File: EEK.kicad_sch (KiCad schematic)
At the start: 40 parts, among them J1 Screw_Terminal_01x02

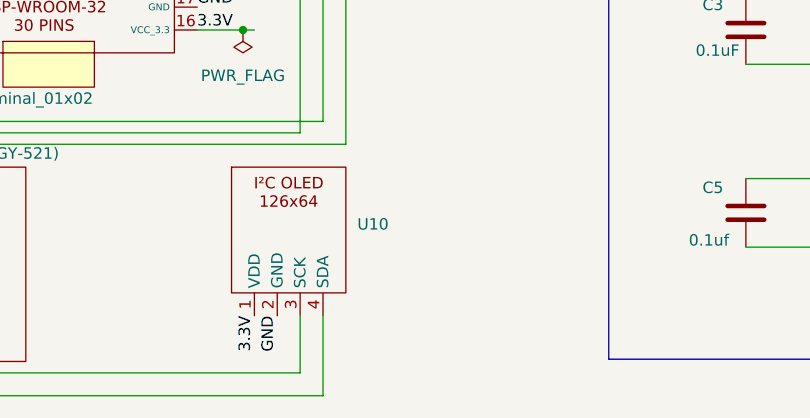
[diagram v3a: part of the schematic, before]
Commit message: add footprint for oled with gnd on pin 1, improve the copper field
Add a second footprint for oled with the gnd on pin 1 instead pin 2. Improve the copper filed
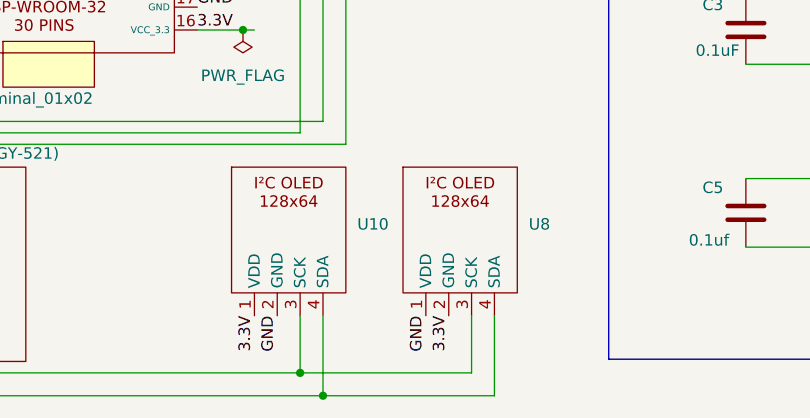
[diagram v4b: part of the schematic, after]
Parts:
- added U8: ~, Connector_PinHeader_2.54mm:PinHeader_1x04_P2.54mm_Vertical, symbol PH_LIB_sym:126x64_I²C_OLED
- U10: footprint TerminalBlock_Phoenix:TerminalBlock_Phoenix_MKDS-1,5-4_1x04_P5.00mm_Horizontal -> Connector_PinHeader_2.54mm:PinHeader_1x04_P2.54mm_Vertical
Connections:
- net 3.3V: now also U8.2 (GND)
- net GND: now also U8.1 (VDD)
- net SCL: now also U8.3 (SCK)
- net SDA: now also U8.4 (SDA)
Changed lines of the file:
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@@
 	)
 	(junction
+		(at 127 124.46)
+		(diameter 0)
+		(color 0 0 0 0)
+	)
+	(junction
+		(at 124.46 121.92)
+		(diameter 0)
+		(color 0 0 0 0)
+	)
+	(junction
 		(at 41.91 64.77)
 		(diameter 0)
@@
 	(wire
 		(pts
+			(xy 127 124.46) (xy 146.05 124.46)
+		)
+		(stroke
+			(width 0)
+			(type default)
+		)
+	)
+	(wire
+		(pts
 			(xy 213.36 80.01) (xy 222.25 80.01)
 		)
@@
 	(wire
 		(pts
+			(xy 143.51 121.92) (xy 143.51 115.57)
+		)
+		(stroke
+			(width 0)
+			(type default)
+		)
+	)
+	(wire
+		(pts
+			(xy 146.05 124.46) (xy 146.05 115.57)
+		)
+		(stroke
+			(width 0)
+			(type default)
+		)
+	)
+	(wire
+		(pts
 			(xy 60.96 72.39) (xy 60.96 68.58)
 		)
@@
 	(wire
 		(pts
+			(xy 124.46 121.92) (xy 143.51 121.92)
+		)
+		(stroke
+			(width 0)
+			(type default)
+		)
+	)
+	(wire
+		(pts
 			(xy 43.18 105.41) (xy 50.8 105.41)
 		)
@@
 	)
 	(label "GND"
+		(at 138.43 115.57 270)
+		(fields_autoplaced yes)
+		(effects
+			(font
+				(size 1.27 1.27)
+			)
+			(justify right bottom)
+		)
+	)
+	(label "GND"
 		(at 222.25 81.28 180)
 		(fields_autoplaced yes)
@@
 		)
 	)
+	(label "3.3V"
+		(at 140.97 115.57 270)
+		(fields_autoplaced yes)
+		(effects
+			(font
+				(size 1.27 1.27)
+			)
+			(justify right bottom)
+		)
+	)
 	(label "GND"
 		(at 49.53 105.41 180)
@@
 			)
 		)
-		(property "Footprint" "TerminalBlock_Phoenix:TerminalBlock_Phoenix_MKDS-1,5-4_1x04_P5.00mm_Horizontal"
+		(property "Footprint" "Connector_PinHeader_2.54mm:PinHeader_1x04_P2.54mm_Vertical"
 			(at 118.11 101.6 0)
 			(effects
@@
 					(unit 1)
 				)
+			)
+		)
+	)
+	(symbol
+		(lib_name "126x64_I²C_OLED_1")
+		(lib_id "PH_LIB_sym:126x64_I²C_OLED")
+		(at 137.16 101.6 0)
+		(unit 1)
+		(exclude_from_sim no)
+		(in_bom yes)
+		(on_board yes)
+		(dnp no)
+		(fields_autoplaced yes)
+		(property "Reference" "U8"
+			(at 149.86 105.4099 0)
+			(effects
+				(font
+					(size 1.27 1.27)
+				)
+				(justify left)
+			)
+		)
+		(property "Value" "~"
+			(at 149.86 107.315 0)
+			(effects
+				(font
+					(size 1.27 1.27)
+				)
+				(justify left)
+			)
+		)
+		(property "Footprint" "Connector_PinHeader_2.54mm:PinHeader_1x04_P2.54mm_Vertical"
+			(at 137.16 101.6 0)
+			(effects
+				(font
+					(size 1.27 1.27)
+				)
+				(hide yes)
+			)
+		)
+		(property "Datasheet" ""
+			(at 137.16 101.6 0)
+			(effects
+				(font
+					(size 1.27 1.27)
+				)
+				(hide yes)
+			)
+		)
+		(property "Description" ""
+			(at 137.16 101.6 0)
+			(effects
+				(font
+					(size 1.27 1.27)
+				)
+				(hide yes)
+			)
+		)
+		(pin "3"
+		)
+		(pin "2"
+		)
+		(pin "4"
+		)
+		(pin "1"
+		)
+		(instances
+			(project "EEK"
+				(path "/0a4f8f30-fcea-49ae-bc76-20e4ae5d80ad"
+					(reference "U8")
+					(unit 1)
+				)

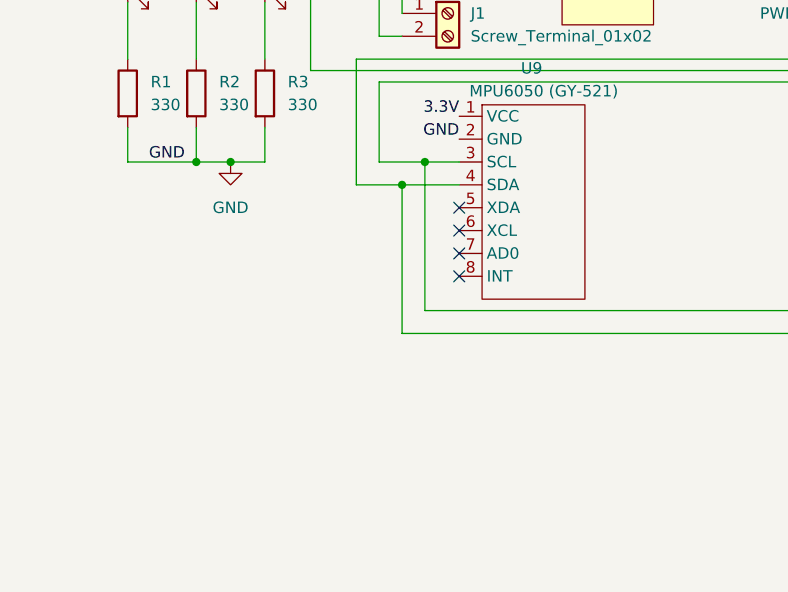
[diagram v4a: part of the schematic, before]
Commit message: improve silkscreen, add capacitors on 3.3V, improve copper filed
improve silkscreen, add capacitors on 3.3V, improve copper filed
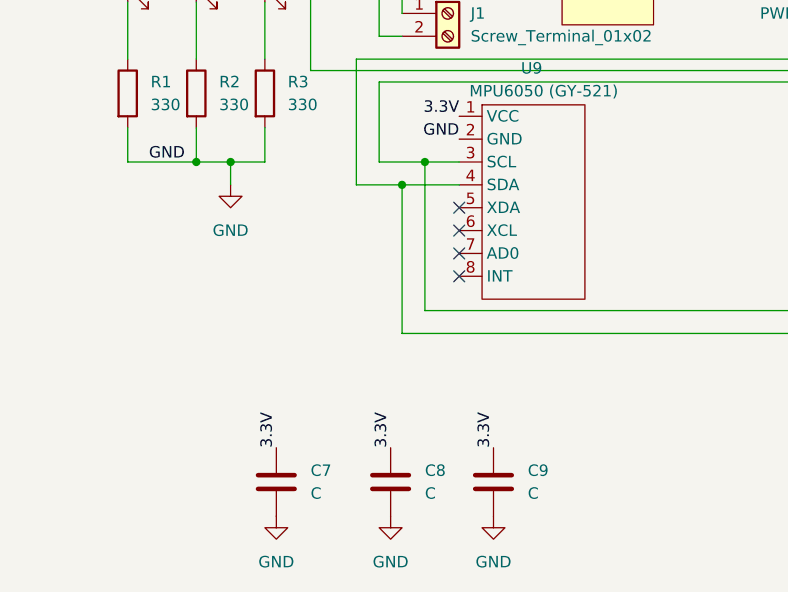
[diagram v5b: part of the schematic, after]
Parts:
- added C7, C8, C9: C, Capacitor_THT:C_Radial_D10.0mm_H12.5mm_P5.00mm, symbol Device:C
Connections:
- net 3.3V: now also C7.1, C8.1, C9.1
- net GND: now also C7.2, C8.2, C9.2

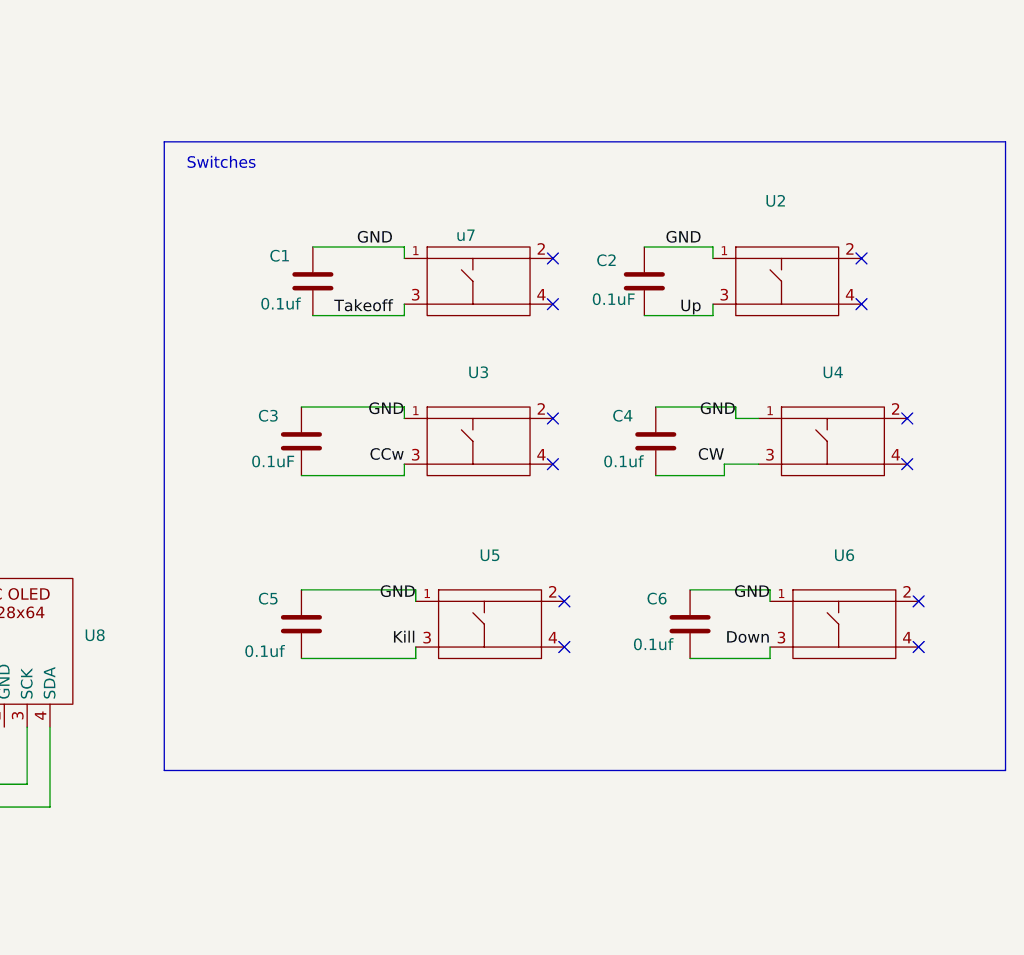
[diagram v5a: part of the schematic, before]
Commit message: add pull down 10K resistors on the switche
add pull down 10K resistors on the switche
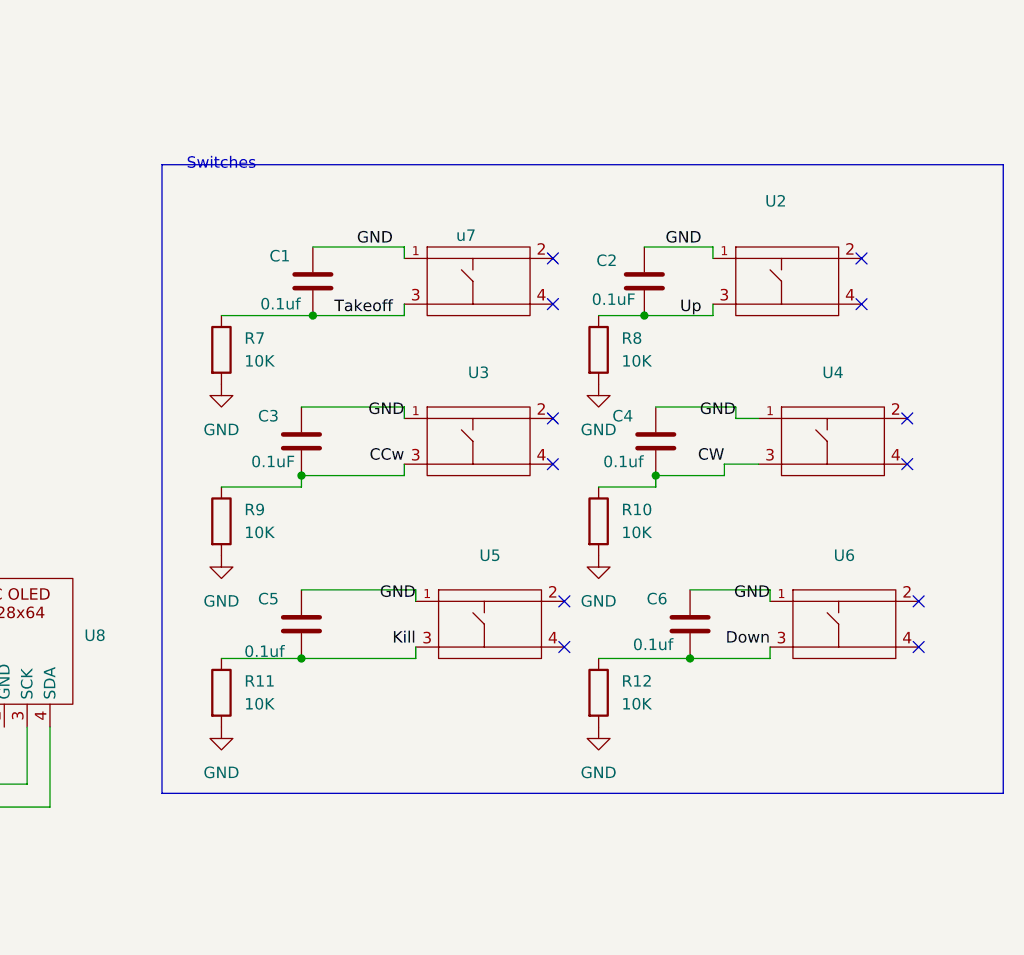
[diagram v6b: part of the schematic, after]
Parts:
- added R10, R11, R12, R7, R8, R9: 10K, Resistor_THT:R_Axial_DIN0207_L6.3mm_D2.5mm_P10.16mm_Horizontal, symbol Device:R
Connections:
- net CCw: now also R9.1
- net CW: now also R10.1
- net Down: now also R12.1
- net GND: now also R10.2, R11.2, R12.2, R7.2, R8.2, R9.2
- net Kill: now also R11.1
- net Takeoff: now also R7.1
- net Up: now also R8.1

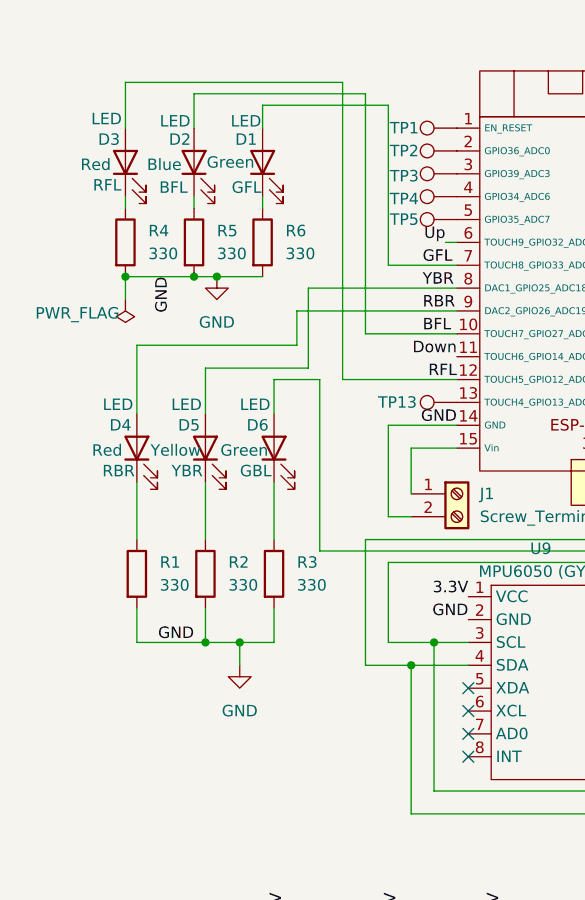
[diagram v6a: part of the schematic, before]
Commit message: Version SMD before introduce SMD foot print
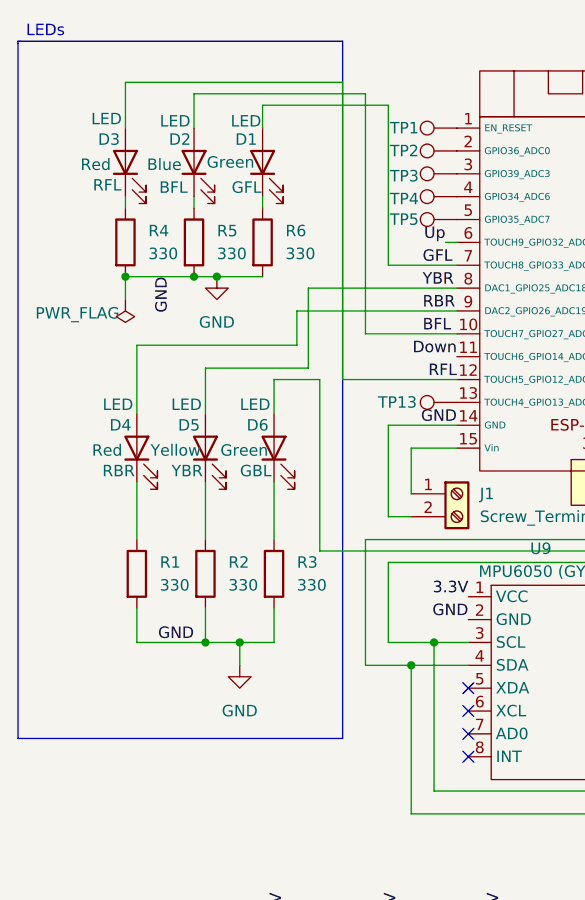
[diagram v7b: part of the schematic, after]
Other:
- note added: "LEDs"
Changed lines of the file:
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@@
+		)
+	)
+	(polyline
+		(pts
+			(xy 29.972 38.608) (xy 30.226 38.608)
+		)
+		(stroke
+			(width 0)
+			(type default)
 		)
 	)
@@
 		)
 	)
+	(polyline
+		(pts
+			(xy 30.226 38.608) (xy 66.04 38.608)
+		)
+		(stroke
+			(width 0)
+			(type default)
+		)
+	)
 	(wire
 		(pts
@@
 		)
 	)
+	(polyline
+		(pts
+			(xy 29.972 38.862) (xy 29.972 116.078)
+		)
+		(stroke
+			(width 0)
+			(type default)
+		)
+	)
 	(wire
 		(pts
@@
 		)
 	)
+	(polyline
+		(pts
+			(xy 66.04 116.078) (xy 29.972 116.078)
+		)
+		(stroke
+			(width 0)
+			(type default)
+		)
+	)
+	(polyline
+		(pts
+			(xy 66.04 38.608) (xy 66.04 116.078)
+		)
+		(stroke
+			(width 0)
+			(type default)
+		)
+	)
 	(wire
 		(pts
@@
 		(pts
 			(xy 71.12 81.28) (xy 78.74 81.28)
+		)
+		(stroke
+			(width 0)
+			(type default)
+		)
+	)
+	(polyline
+		(pts
+			(xy 29.972 38.862) (xy 29.972 38.608)
 		)
 		(stroke
@@
 		(effects
 			(font
+				(size 1.27 1.27)
+			)
+		)
+	)
+	(text "LEDs"
+		(exclude_from_sim no)
+		(at 33.02 37.592 0)
+		(effects
+			(font

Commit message: Change footprint to SMD
Change footprint to SMD
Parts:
- C1, C2, C3, C4, C5, C6: footprint Capacitor_THT:C_Disc_D8.0mm_W2.5mm_P5.00mm -> Capacitor_SMD:C_0805_2012Metric
- C7, C8, C9: footprint Capacitor_THT:C_Radial_D10.0mm_H12.5mm_P5.00mm -> Capacitor_SMD:C_Elec_10x10.2
- D1, D2, D3, D4, D5, D6: footprint LED_THT:LED_D5.0mm -> LED_SMD:LED_0805_2012Metric_Pad1.15x1.40mm_HandSolder
- R1, R10, R11, R12, R2, R3, R4, R5, R6, R7, R8, R9: footprint Resistor_THT:R_Axial_DIN0207_L6.3mm_D2.5mm_P10.16mm_Horizontal -> Resistor_SMD:R_0805_2012Metric
- U2, U3, U4, U5, U6, u7: footprint PH_lib:SW_Tactile -> Button_Switch_SMD:SW_SPST_TL3305A
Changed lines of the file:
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@@
 			)
 		)
-		(property "Footprint" "LED_THT:LED_D5.0mm"
+		(property "Footprint" "LED_SMD:LED_0805_2012Metric_Pad1.15x1.40mm_HandSolder"
 			(at 50.8 83.82 0)
 			(effects
@@
 			)
 		)
-		(property "Footprint" "Resistor_THT:R_Axial_DIN0207_L6.3mm_D2.5mm_P10.16mm_Horizontal"
+		(property "Footprint" "Resistor_SMD:R_0805_2012Metric"
 			(at 163.322 92.71 90)
 			(effects
@@
 			)
 		)
-		(property "Footprint" "Resistor_THT:R_Axial_DIN0207_L6.3mm_D2.5mm_P10.16mm_Horizontal"
+		(property "Footprint" "Resistor_SMD:R_0805_2012Metric"
 			(at 40.132 60.96 90)
 			(effects
@@
 			)
 		)
-		(property "Footprint" "LED_THT:LED_D5.0mm"
+		(property "Footprint" "LED_SMD:LED_0805_2012Metric_Pad1.15x1.40mm_HandSolder"
 			(at 49.53 52.07 0)
 			(effects
@@
 			)
 		)
-		(property "Footprint" "Capacitor_THT:C_Disc_D8.0mm_W2.5mm_P5.00mm"
+		(property "Footprint" "Capacitor_SMD:C_0805_2012Metric"
 			(at 174.9552 107.95 0)
 			(effects
@@
 			)
 		)
-		(property "Footprint" "Resistor_THT:R_Axial_DIN0207_L6.3mm_D2.5mm_P10.16mm_Horizontal"
+		(property "Footprint" "Resistor_SMD:R_0805_2012Metric"
 			(at 205.232 111.76 90)
 			(effects
@@
 			)
 		)
-		(property "Footprint" "LED_THT:LED_D5.0mm"
+		(property "Footprint" "LED_SMD:LED_0805_2012Metric_Pad1.15x1.40mm_HandSolder"
 			(at 57.15 52.07 0)
 			(effects
@@
 			)
 		)
-		(property "Footprint" "Resistor_THT:R_Axial_DIN0207_L6.3mm_D2.5mm_P10.16mm_Horizontal"
+		(property "Footprint" "Resistor_SMD:R_0805_2012Metric"
 			(at 205.232 92.71 90)
 			(effects
@@
 			)
 		)
-		(property "Footprint" "Capacitor_THT:C_Disc_D8.0mm_W2.5mm_P5.00mm"
+		(property "Footprint" "Capacitor_SMD:C_0805_2012Metric"
 			(at 176.2252 69.85 0)
 			(effects
@@
 			)
 		)
-		(property "Footprint" "PH_lib:SW_Tactile"
+		(property "Footprint" "Button_Switch_SMD:SW_SPST_TL3305A"
 			(at 189.23 59.69 0)
 			(effects
@@
 			)
 		)
-		(property "Footprint" "LED_THT:LED_D5.0mm"
+		(property "Footprint" "LED_SMD:LED_0805_2012Metric_Pad1.15x1.40mm_HandSolder"
 			(at 43.18 83.82 0)
 			(effects
@@
 			)
 		)
-		(property "Footprint" "PH_lib:SW_Tactile"
+		(property "Footprint" "Button_Switch_SMD:SW_SPST_TL3305A"
 			(at 223.52 59.69 0)
 			(effects
@@
 			)
 		)
-		(property "Footprint" "PH_lib:SW_Tactile"
+		(property "Footprint" "Button_Switch_SMD:SW_SPST_TL3305A"
 			(at 189.23 77.47 0)
 			(effects
@@
 			)
 		)
-		(property "Footprint" "PH_lib:SW_Tactile"
+		(property "Footprint" "Button_Switch_SMD:SW_SPST_TL3305A"
 			(at 190.5 97.79 0)
 			(effects
@@
 			)
 		)
-		(property "Footprint" "LED_THT:LED_D5.0mm"
+		(property "Footprint" "LED_SMD:LED_0805_2012Metric_Pad1.15x1.40mm_HandSolder"
 			(at 41.91 52.07 0)
 			(effects
@@
 			)
 		)
-		(property "Footprint" "Resistor_THT:R_Axial_DIN0207_L6.3mm_D2.5mm_P10.16mm_Horizontal"
+		(property "Footprint" "Resistor_SMD:R_0805_2012Metric"
 			(at 205.232 73.66 90)
 			(effects
@@
 			)
 		)
-		(property "Footprint" "Resistor_THT:R_Axial_DIN0207_L6.3mm_D2.5mm_P10.16mm_Horizontal"
+		(property "Footprint" "Resistor_SMD:R_0805_2012Metric"
 			(at 55.372 60.96 90)
 			(effects
@@
 			)
 		)
-		(property "Footprint" "Capacitor_THT:C_Radial_D10.0mm_H12.5mm_P5.00mm"
+		(property "Footprint" "Capacitor_SMD:C_Elec_10x10.2"
 			(at 60.6552 144.78 0)
 			(effects
@@
 			)
 		)
-		(property "Footprint" "Resistor_THT:R_Axial_DIN0207_L6.3mm_D2.5mm_P10.16mm_Horizontal"
+		(property "Footprint" "Resistor_SMD:R_0805_2012Metric"
 			(at 41.402 97.79 90)
 			(effects
@@
 			)
 		)
-		(property "Footprint" "Resistor_THT:R_Axial_DIN0207_L6.3mm_D2.5mm_P10.16mm_Horizontal"
+		(property "Footprint" "Resistor_SMD:R_0805_2012Metric"
 			(at 163.322 73.66 90)
 			(effects
@@
 			)
 		)
-		(property "Footprint" "Capacitor_THT:C_Disc_D8.0mm_W2.5mm_P5.00mm"
+		(property "Footprint" "Capacitor_SMD:C_0805_2012Metric"
 			(at 214.3252 87.63 0)
 			(effects
@@
 			)
 		)
-		(property "Footprint" "Capacitor_THT:C_Radial_D10.0mm_H12.5mm_P5.00mm"
+		(property "Footprint" "Capacitor_SMD:C_Elec_10x10.2"
 			(at 84.7852 144.78 0)
 			(effects
@@
 			)
 		)
-		(property "Footprint" "Capacitor_THT:C_Radial_D10.0mm_H12.5mm_P5.00mm"
+		(property "Footprint" "Capacitor_SMD:C_Elec_10x10.2"
 			(at 73.3552 144.78 0)
 			(effects
@@
 			)
 		)
-		(property "Footprint" "Capacitor_THT:C_Disc_D8.0mm_W2.5mm_P5.00mm"
+		(property "Footprint" "Capacitor_SMD:C_0805_2012Metric"
 			(at 218.1352 107.95 0)
 			(effects
@@
 			)
 		)
-		(property "Footprint" "Resistor_THT:R_Axial_DIN0207_L6.3mm_D2.5mm_P10.16mm_Horizontal"
+		(property "Footprint" "Resistor_SMD:R_0805_2012Metric"
 			(at 49.022 97.79 90)
 			(effects
@@
 			)
 		)
-		(property "Footprint" "Resistor_THT:R_Axial_DIN0207_L6.3mm_D2.5mm_P10.16mm_Horizontal"
+		(property "Footprint" "Resistor_SMD:R_0805_2012Metric"
 			(at 47.752 60.96 90)
 			(effects
@@
 			)
 		)
-		(property "Footprint" "PH_lib:SW_Tactile"
+		(property "Footprint" "Button_Switch_SMD:SW_SPST_TL3305A"
 			(at 228.6 77.47 0)
 			(effects
@@
 			)
 		)
-		(property "Footprint" "Capacitor_THT:C_Disc_D8.0mm_W2.5mm_P5.00mm"
+		(property "Footprint" "Capacitor_SMD:C_0805_2012Metric"
 			(at 174.9552 87.63 0)
 			(effects
@@
 			)
 		)
-		(property "Footprint" "Capacitor_THT:C_Disc_D8.0mm_W2.5mm_P5.00mm"
+		(property "Footprint" "Capacitor_SMD:C_0805_2012Metric"
 			(at 213.0552 69.85 0)
 			(effects
@@
 			)
 		)
-		(property "Footprint" "Resistor_THT:R_Axial_DIN0207_L6.3mm_D2.5mm_P10.16mm_Horizontal"
+		(property "Footprint" "Resistor_SMD:R_0805_2012Metric"
 			(at 163.322 111.76 90)
 			(effects
@@
 			)
 		)
-		(property "Footprint" "LED_THT:LED_D5.0mm"
+		(property "Footprint" "LED_SMD:LED_0805_2012Metric_Pad1.15x1.40mm_HandSolder"
 			(at 58.42 83.82 0)
 			(effects
@@
 			)
 		)
-		(property "Footprint" "Resistor_THT:R_Axial_DIN0207_L6.3mm_D2.5mm_P10.16mm_Horizontal"
+		(property "Footprint" "Resistor_SMD:R_0805_2012Metric"
 			(at 56.642 97.79 90)
 			(effects
@@
 			)
 		)
-		(property "Footprint" "PH_lib:SW_Tactile"
+		(property "Footprint" "Button_Switch_SMD:SW_SPST_TL3305A"
 			(at 229.87 97.79 0)
 			(effects
